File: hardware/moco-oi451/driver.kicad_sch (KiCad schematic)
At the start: 38 parts, among them U4 LM4040A50

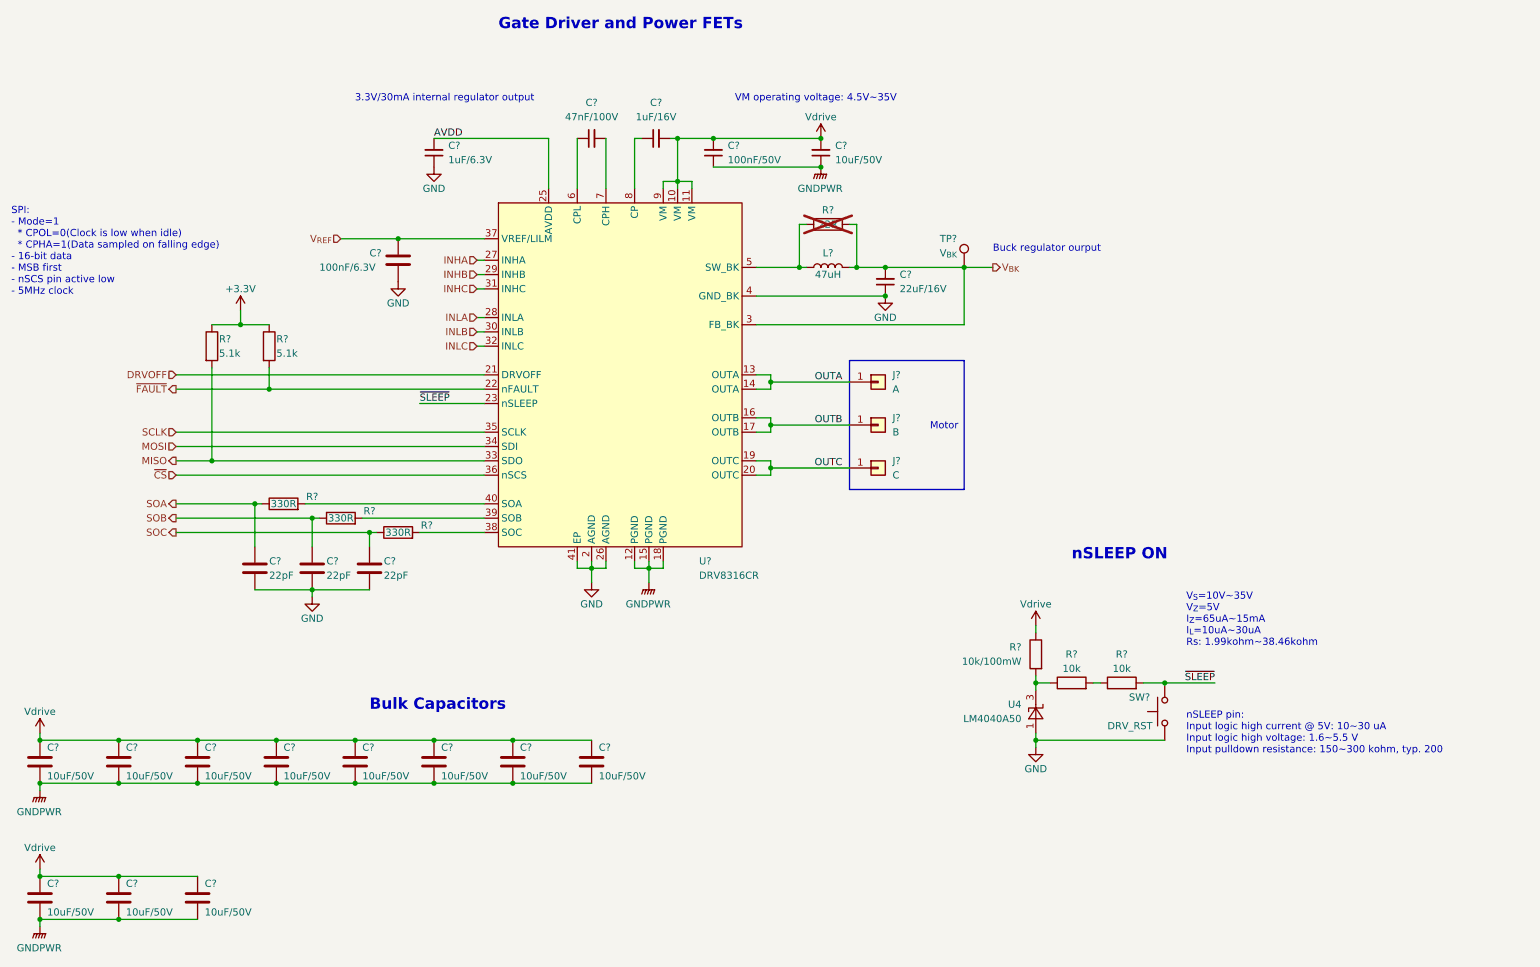
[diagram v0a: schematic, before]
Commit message: Reroute and reduce size to Ø40mm
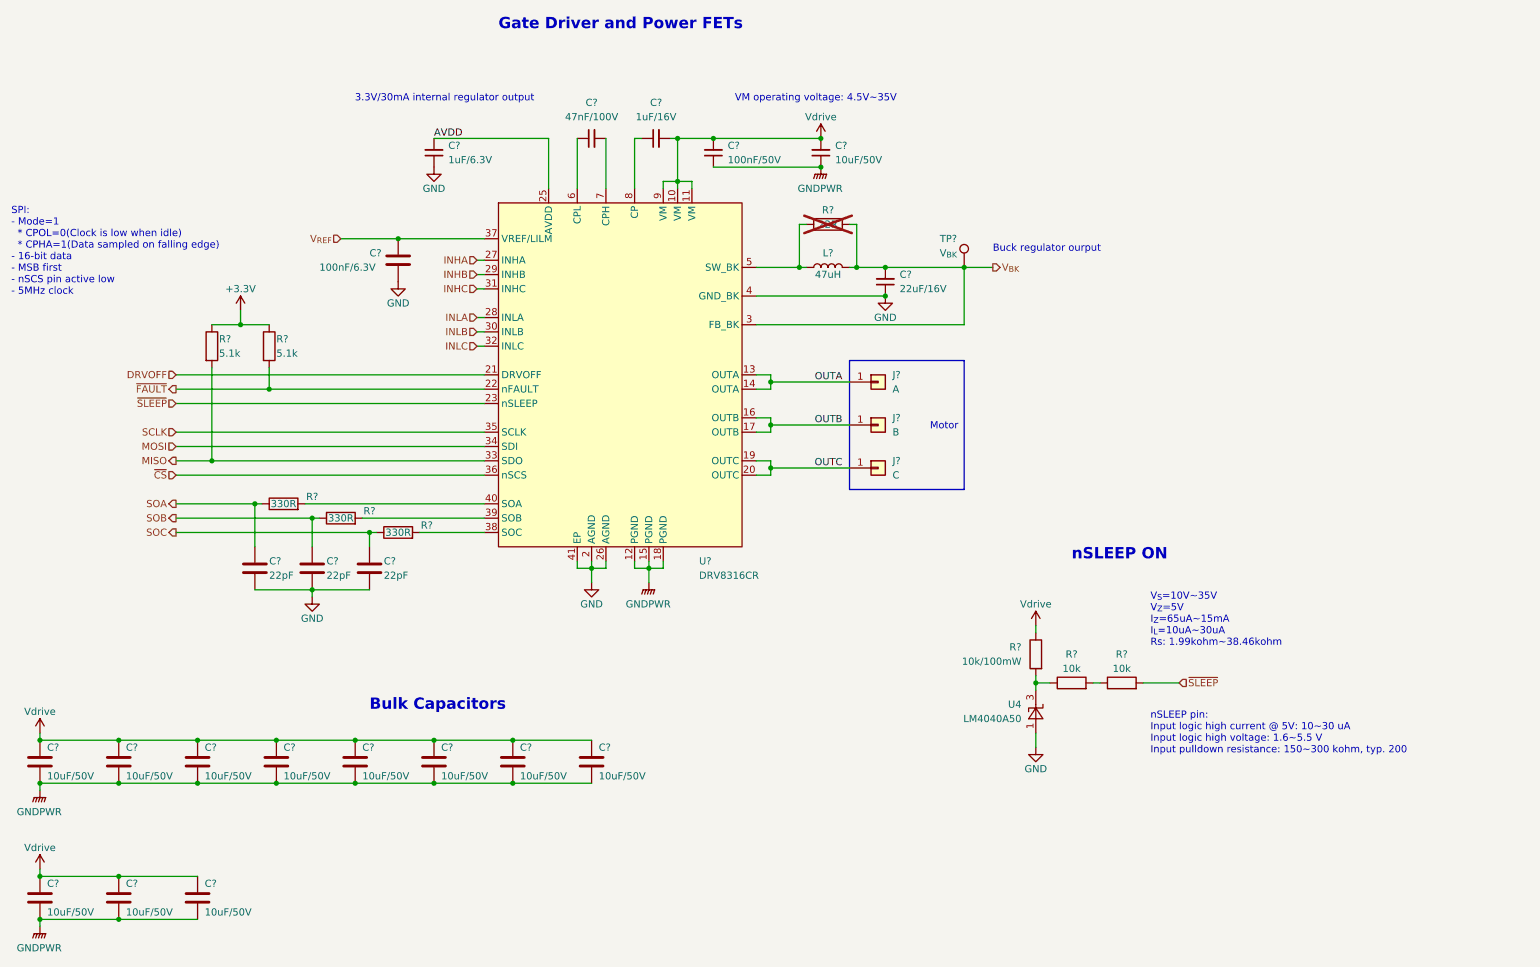
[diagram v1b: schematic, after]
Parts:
- removed SW?: DRV_RST, Button_Switch_SMD:SW_SPST_TL3342, symbol Switch:SW_Push
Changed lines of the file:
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@@
   (junction (at 140.97 46.99) (diameter 0) (color 0 0 0 0)
   )
-  (junction (at 227.33 143.51) (diameter 0) (color 0 0 0 0)
-  )
   (junction (at 140.97 54.61) (diameter 0) (color 0 0 0 0)
   )
@@
   (junction (at 204.47 143.51) (diameter 0) (color 0 0 0 0)
   )
-  (junction (at 204.47 153.67) (diameter 0) (color 0 0 0 0)
-  )
   (junction (at 41.91 185.42) (diameter 0) (color 0 0 0 0)
   )
@@
     (stroke (width 0) (type default))
   )
-  (wire (pts (xy 223.52 143.51) (xy 227.33 143.51))
+  (wire (pts (xy 223.52 143.51) (xy 229.87 143.51))
     (stroke (width 0) (type default))
   )
@@
     (stroke (width 0) (type default))
   )
-  (wire (pts (xy 204.47 154.94) (xy 204.47 153.67))
+  (wire (pts (xy 204.47 152.4) (xy 204.47 154.94))
     (stroke (width 0) (type default))
   )
@@
     (stroke (width 0) (type default))
   )
-  (wire (pts (xy 95.25 93.98) (xy 106.68 93.98))
+  (wire (pts (xy 52.07 93.98) (xy 106.68 93.98))
     (stroke (width 0) (type default))
   )
@@
     (stroke (width 0) (type default))
   )
-  (wire (pts (xy 204.47 153.67) (xy 204.47 152.4))
-    (stroke (width 0) (type default))
-  )
   (wire (pts (xy 27.94 152.4) (xy 27.94 153.67))
     (stroke (width 0) (type default))
@@
     (stroke (width 0) (type default))
   )
-  (wire (pts (xy 227.33 143.51) (xy 236.22 143.51))
-    (stroke (width 0) (type default))
-  )
   (wire (pts (xy 157.48 104.14) (xy 157.48 105.41))
     (stroke (width 0) (type default))
@@
   )
   (wire (pts (xy 52.07 104.14) (xy 58.42 104.14))
-    (stroke (width 0) (type default))
-  )
-  (wire (pts (xy 204.47 153.67) (xy 227.33 153.67))
     (stroke (width 0) (type default))
   )
@@
   )
   (text "V_{S}=10V~35V\nV_{Z}=5V\nI_{Z}=65uA~15mA\nI_{L}=10uA~30uA\nRs: 1.99kohm~38.46kohm"
-    (at 231.14 137.16 0)
+    (at 224.79 137.16 0)
     (effects (font (size 1.27 1.27)) (justify left bottom))
   )
@@
   )
   (text "nSLEEP pin:\nInput logic high current @ 5V: 10~30 uA\nInput logic high voltage: 1.6~5.5 V\nInput pulldown resistance: 150~300 kohm, typ. 200"
-    (at 231.14 156.21 0)
+    (at 224.79 156.21 0)
     (effects (font (size 1.27 1.27)) (justify left bottom))
   )
@@
     (effects (font (size 1.27 1.27)) (justify right bottom))
   )
-  (label "~{SLEEP}" (at 236.22 143.51 180) (fields_autoplaced)
-    (effects (font (size 1.27 1.27)) (justify right bottom))
-  )
   (label "OUTC" (at 170.18 105.41 180) (fields_autoplaced)
     (effects (font (size 1.27 1.27)) (justify right bottom))
@@
     (effects (font (size 1.27 1.27)) (justify right bottom))
   )
-  (label "~{SLEEP}" (at 95.25 93.98 0) (fields_autoplaced)
-    (effects (font (size 1.27 1.27)) (justify left bottom))
-  )
   (hierarchical_label "SOC" (shape output) (at 52.07 116.84 180) (fields_autoplaced)
     (effects (font (size 1.27 1.27)) (justify right))
   )
+  (hierarchical_label "~{SLEEP}" (shape input) (at 52.07 93.98 180) (fields_autoplaced)
+    (effects (font (size 1.27 1.27)) (justify right))
+  )
   (hierarchical_label "V_{REF}" (shape input) (at 81.28 64.77 180) (fields_autoplaced)
     (effects (font (size 1.27 1.27)) (justify right))
@@
   (hierarchical_label "INHA" (shape input) (at 105.41 68.58 180) (fields_autoplaced)
     (effects (font (size 1.27 1.27)) (justify right))
+  )
+  (hierarchical_label "~{SLEEP}" (shape input) (at 229.87 143.51 0) (fields_autoplaced)
+    (effects (font (size 1.27 1.27)) (justify left))
   )
   (hierarchical_label "V_{BK}" (shape output) (at 196.85 69.85 0) (fields_autoplaced)
@@
         )
       )
-    )
-  )
-  (symbol (lib_id "Switch:SW_Push") (at 227.33 148.59 90) (unit 1)
-    (in_bom yes) (on_board yes) (dnp no)
-    (property "Reference" "SW?" (at 220.98 146.05 90)
-      (effects (font (size 1.27 1.27)) (justify right))
-    )
-    (property "Value" "DRV_RST" (at 217.17 151.13 90)
-      (effects (font (size 1.27 1.27)) (justify right))
-    )
-    (property "Footprint" "Button_Switch_SMD:SW_SPST_TL3342" (at 222.25 148.59 0)
-      (effects (font (size 1.27 1.27)) hide)
-    )
-    (property "Datasheet" "~" (at 222.25 148.59 0)
-      (effects (font (size 1.27 1.27)) hide)
-    )
-    (pin "1")
-    (pin "2")
-    (instances
-      (project "moco-oi451"
-        (path "/171831cd-2a0d-47b9-8420-65898c688d08/8c626c9e-bc00-4eb5-9b1c-4380247b0f28"
-          (reference "SW?") (unit 1)
-        )
-        (path "/171831cd-2a0d-47b9-8420-65898c688d08/e49edf63-a462-4dde-9ddc-a334d0522771"
-          (reference "SW2") (unit 1)
-        )
-      )
-      (project "moco-od501"
-        (path "/6af178d2-5089-4f26-a9dd-467044aa844a/5f858a64-8e5c-4641-b09d-942a81494abe"
-          (reference "SW?") (unit 1)
-        )
-      )

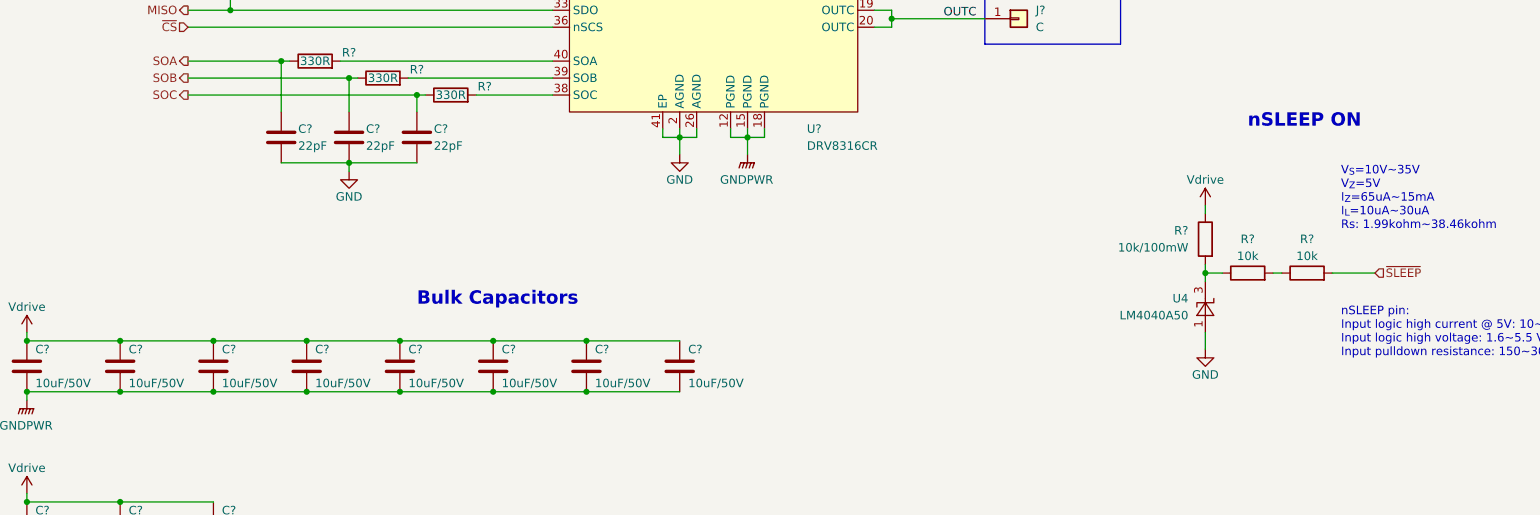
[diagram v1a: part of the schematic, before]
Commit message: Optimize routing
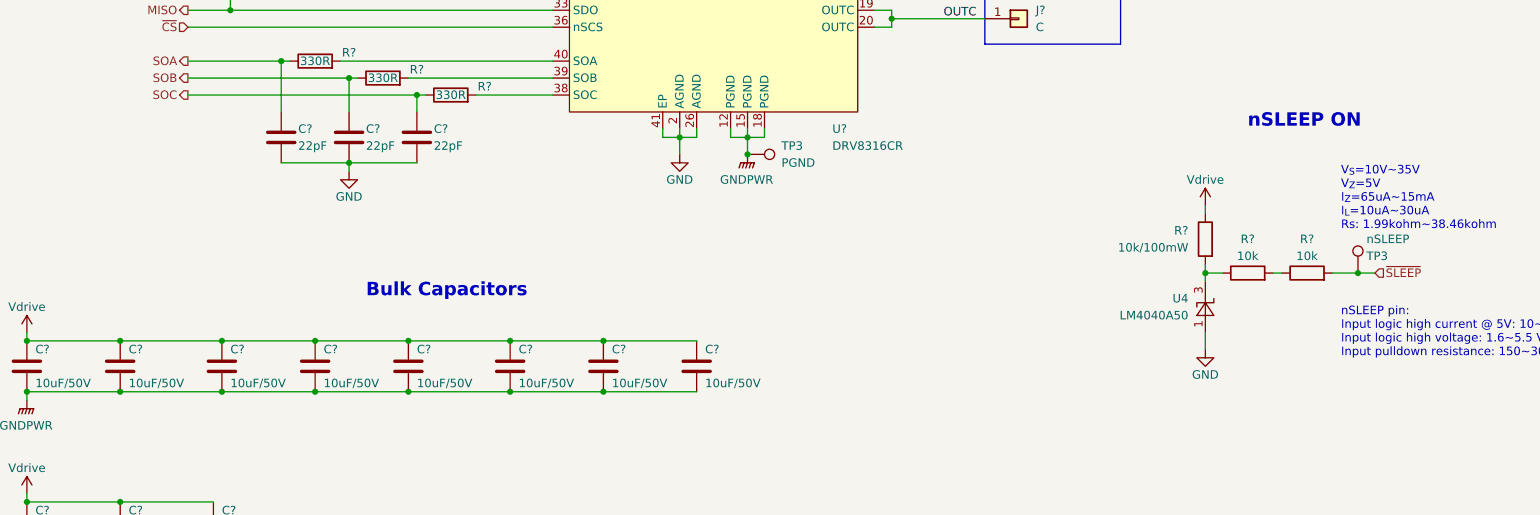
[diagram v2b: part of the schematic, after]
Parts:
- added TP3: PGND, TestPoint:TestPoint_Pad_D1.0mm, symbol Connector:TestPoint
- added TP3: nSLEEP, TestPoint:TestPoint_Pad_D1.0mm, symbol Connector:TestPoint
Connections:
- net GNDPWR: now also TP3.1
- net ~{SLEEP}: now also TP3.1
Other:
- moved on the sheet: C?
